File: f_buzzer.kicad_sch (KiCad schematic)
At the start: 11 parts, among them J1 Conn_01x03, U1 SN74123N

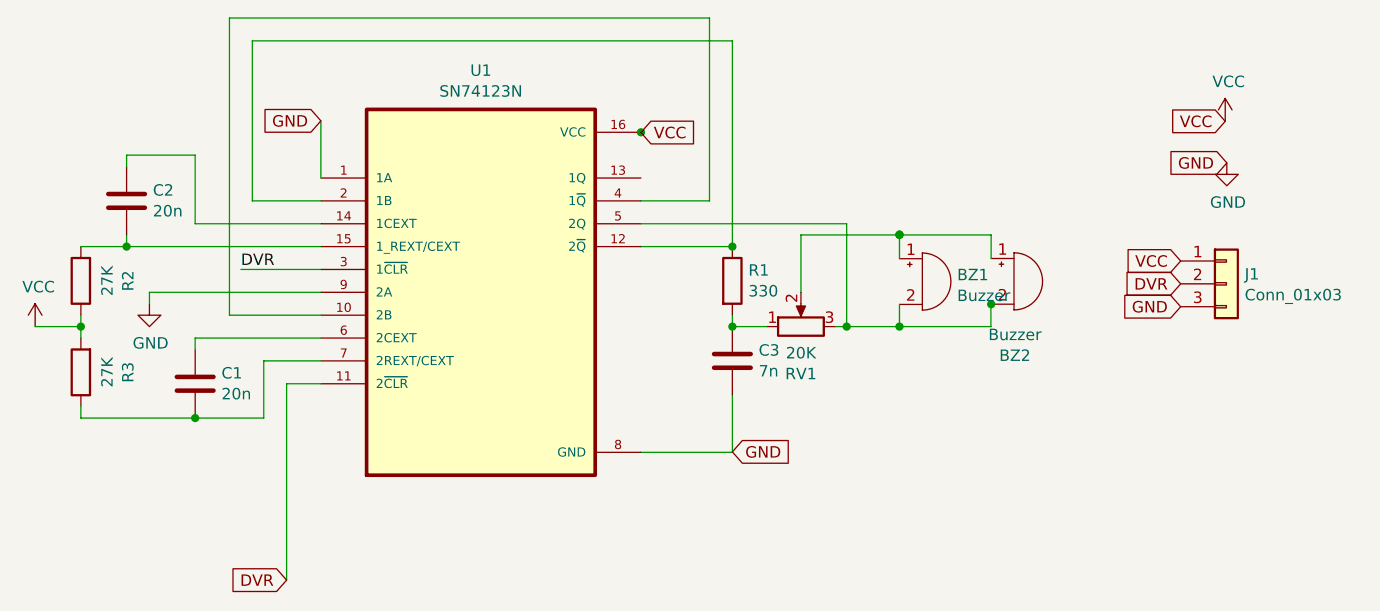
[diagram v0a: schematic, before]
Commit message: Rearranged the components
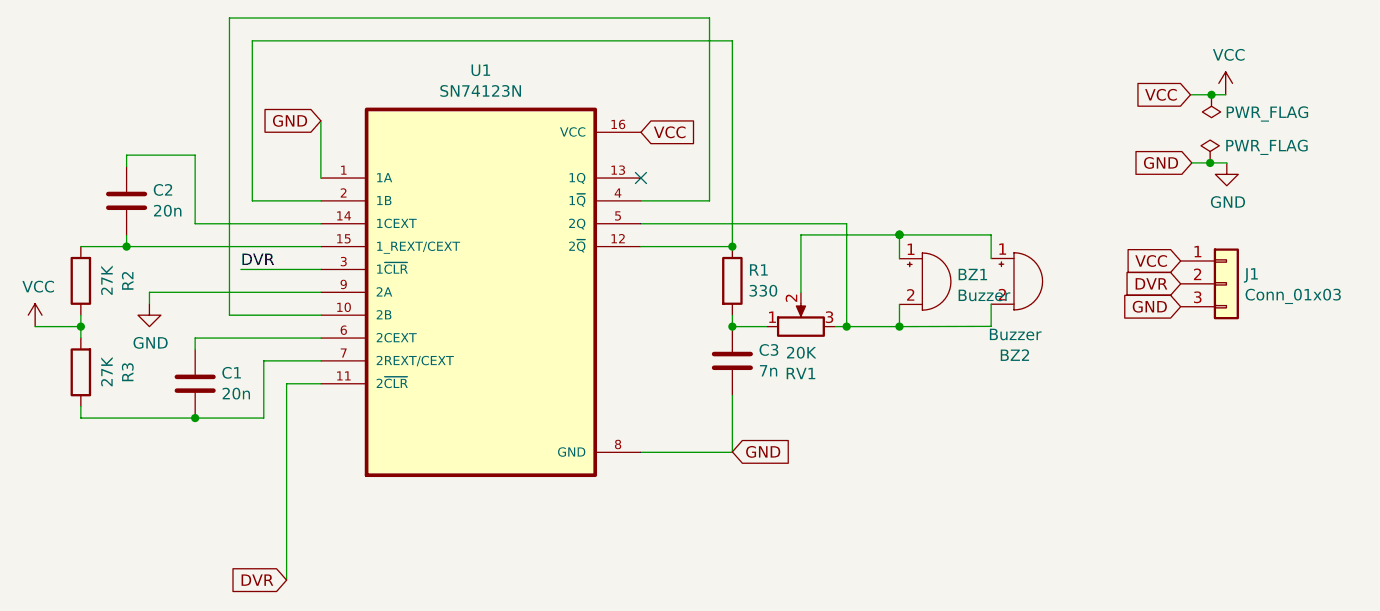
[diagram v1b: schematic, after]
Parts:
- RV1: symbol Device:R_POT -> Device:R_Potentiometer
- U1: footprint Package_DIP:DIP-16_W7.62mm -> Package_DIP:DIP-16_W7.62mm_Socket
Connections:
- net VCC: now also U1.16 (VCC)
- net at BZ2.2 (+): now also BZ1.2 (+), RV1.3, U1.5 (2Q)
- no-connect marks 0 -> 1
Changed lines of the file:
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@@
   (junction (at 114.3 116.84) (diameter 0) (color 0 0 0 0)
   )
+  (junction (at 227.2284 80.9244) (diameter 0) (color 0 0 0 0)
+  )
   (junction (at 173.99 106.68) (diameter 0) (color 0 0 0 0)
   )
-  (junction (at 163.83 85.09) (diameter 0) (color 0 0 0 0)
-  )
   (junction (at 192.5574 96.4946) (diameter 0) (color 0 0 0 0)
   )
@@
   (junction (at 192.5574 106.68) (diameter 0) (color 0 0 0 0)
   )
-  (junction (at 202.7428 104.1908) (diameter 0) (color 0 0 0 0)
+  (junction (at 227.076 88.4936) (diameter 0) (color 0 0 0 0)
   )
   (junction (at 101.6 106.68) (diameter 0) (color 0 0 0 0)
   )
+  (no_connect (at 163.83 90.17))
   (wire (pts (xy 128.27 113.03) (xy 124.46 113.03))
     (stroke (width 0) (type default) (color 0 0 0 0))
@@
     (stroke (width 0) (type default) (color 0 0 0 0))
   )
+  (wire (pts (xy 224.8916 80.9244) (xy 227.2284 80.9244))
+    (stroke (width 0) (type default) (color 0 0 0 0))
+  )
+  (wire (pts (xy 227.076 88.4936) (xy 228.9302 88.4936))
+    (stroke (width 0) (type default) (color 0 0 0 0))
+  )
   (wire (pts (xy 181.61 96.4946) (xy 181.61 102.87))
     (stroke (width 0) (type default) (color 0 0 0 0))
@@
     (stroke (width 0) (type default) (color 0 0 0 0))
   )
+  (wire (pts (xy 227.2284 80.9244) (xy 228.8032 80.9244))
+    (stroke (width 0) (type default) (color 0 0 0 0))
+  )
   (wire (pts (xy 124.46 113.03) (xy 124.46 134.8486))
     (stroke (width 0) (type default) (color 0 0 0 0))
@@
     (stroke (width 0) (type default) (color 0 0 0 0))
   )
-  (wire (pts (xy 202.7174 106.68) (xy 202.7174 104.2162))
+  (wire (pts (xy 202.7428 106.6546) (xy 202.7428 104.1908))
     (stroke (width 0) (type default) (color 0 0 0 0))
   )
@@
     (stroke (width 0) (type default) (color 0 0 0 0))
   )
-  (wire (pts (xy 192.5574 106.68) (xy 202.7174 106.68))
+  (wire (pts (xy 192.5574 106.68) (xy 202.7428 106.6546))
     (stroke (width 0) (type default) (color 0 0 0 0))
   )
@@
     (stroke (width 0) (type default) (color 0 0 0 0))
   )
-  (wire (pts (xy 163.7792 85.0646) (xy 163.7792 85.09))
-    (stroke (width 0) (type default) (color 0 0 0 0))
-  )
   (wire (pts (xy 163.83 95.25) (xy 186.69 95.25))
     (stroke (width 0) (type default) (color 0 0 0 0))
   )
-  (wire (pts (xy 163.7792 85.09) (xy 163.7284 85.09))
+  (wire (pts (xy 225.044 88.4936) (xy 227.076 88.4936))
     (stroke (width 0) (type default) (color 0 0 0 0))
   )
@@
     )
   )
-  (global_label "GND" (shape input) (at 228.9302 88.4936 180) (fields_autoplaced)
+  (global_label "GND" (shape input) (at 225.044 88.4936 180) (fields_autoplaced)
+    (effects (font (size 1.27 1.27)) (justify right))
+    (property "Intersheet References" "${INTERSHEET_REFS}" (id 0) (at -3.8862 0 0)
+      (effects (font (size 1.27 1.27)) hide)
+    )
+  )
+  (global_label "GND" (shape input) (at 223.7994 104.4702 180) (fields_autoplaced)
     (effects (font (size 1.27 1.27)) (justify right))
     (property "Intersheet References" "${INTERSHEET_REFS}" (id 0) (at 0 0 0)
@@
     )
   )
-  (global_label "GND" (shape input) (at 223.7994 104.4702 180) (fields_autoplaced)
+  (global_label "DVR" (shape input) (at 223.7994 101.9302 180) (fields_autoplaced)
     (effects (font (size 1.27 1.27)) (justify right))
     (property "Intersheet References" "${INTERSHEET_REFS}" (id 0) (at 0 0 0)
@@
     )
   )
-  (global_label "DVR" (shape input) (at 223.7994 101.9302 180) (fields_autoplaced)
+  (global_label "GND" (shape input) (at 128.27 83.82 180) (fields_autoplaced)
     (effects (font (size 1.27 1.27)) (justify right))
     (property "Intersheet References" "${INTERSHEET_REFS}" (id 0) (at 0 0 0)
@@
     )
   )
-  (global_label "GND" (shape input) (at 128.27 83.82 180) (fields_autoplaced)
-    (effects (font (size 1.27 1.27)) (justify right))
-    (property "Intersheet References" "${INTERSHEET_REFS}" (id 0) (at 0 0 0)
-      (effects (font (size 1.27 1.27)) hide)
-    )
-  )
-  (global_label "VCC" (shape input) (at 228.7524 83.8708 180) (fields_autoplaced)
-    (effects (font (size 1.27 1.27)) (justify right))
-    (property "Intersheet References" "${INTERSHEET_REFS}" (id 0) (at 0 0 0)
-      (effects (font (size 1.27 1.27)) hide)
-    )
-  )
-  (global_label "VCC" (shape input) (at 163.83 85.1154 0) (fields_autoplaced)
+  (global_label "VCC" (shape input) (at 224.8916 80.9244 180) (fields_autoplaced)
+    (effects (font (size 1.27 1.27)) (justify right))
+    (property "Intersheet References" "${INTERSHEET_REFS}" (id 0) (at -3.8608 -2.9464 0)
+      (effects (font (size 1.27 1.27)) hide)
+    )
+  )
+  (global_label "VCC" (shape input) (at 163.83 85.09 0) (fields_autoplaced)
     (effects (font (size 1.27 1.27)) (justify left))
-    (property "Intersheet References" "${INTERSHEET_REFS}" (id 0) (at 0 0 0)
+    (property "Intersheet References" "${INTERSHEET_REFS}" (id 0) (at 0 -0.0254 0)
       (effects (font (size 1.27 1.27)) hide)
     )
@@
     (pin "2")
   )
-  (symbol (lib_id "Device:R_POT") (at 181.61 106.68 90) (unit 1)
+  (symbol (lib_id "Device:R_Potentiometer") (at 181.61 106.68 90) (unit 1)
     (in_bom yes) (on_board yes)
     (property "Reference" "RV1" (id 0) (at 181.61 111.9378 90))
@@
     (property "Reference" "U1" (id 0) (at 146.05 78.232 0))
     (property "Value" "SN74123N" (id 1) (at 146.05 80.5434 0))
-    (property "Footprint" "Package_DIP:DIP-16_W7.62mm" (id 2) (at 146.05 102.87 0)
+    (property "Footprint" "Package_DIP:DIP-16_W7.62mm_Socket" (id 2) (at 146.05 102.87 0)
       (effects (font (size 1.27 1.27)) (justify left bottom) hide)
     )
@@
     (pin "3")
   )
-  (symbol (lib_id "power:VCC") (at 228.7524 83.8708 0) (unit 1)
-    (in_bom yes) (on_board yes)
-    (property "Reference" "#PWR?" (id 0) (at 228.7524 87.6808 0)
-      (effects (font (size 1.27 1.27)) hide)
-    )
-    (property "Value" "VCC" (id 1) (at 229.1334 79.4766 0))
-    (property "Footprint" "" (id 2) (at 228.7524 83.8708 0)
-      (effects (font (size 1.27 1.27)) hide)
-    )
-    (property "Datasheet" "" (id 3) (at 228.7524 83.8708 0)
+  (symbol (lib_id "power:VCC") (at 228.8032 80.9244 0) (unit 1)
+    (in_bom yes) (on_board yes)
+    (property "Reference" "#PWR0101" (id 0) (at 228.8032 84.7344 0)
+      (effects (font (size 1.27 1.27)) hide)
+    )
+    (property "Value" "VCC" (id 1) (at 229.1842 76.5302 0))
+    (property "Footprint" "" (id 2) (at 228.8032 80.9244 0)
+      (effects (font (size 1.27 1.27)) hide)
+    )
+    (property "Datasheet" "" (id 3) (at 228.8032 80.9244 0)
       (effects (font (size 1.27 1.27)) hide)
     )
@@
   (symbol (lib_id "power:GND") (at 228.9302 88.4936 0) (unit 1)
     (in_bom yes) (on_board yes)
-    (property "Reference" "#PWR?" (id 0) (at 228.9302 94.8436 0)
+    (property "Reference" "#PWR0102" (id 0) (at 228.9302 94.8436 0)
       (effects (font (size 1.27 1.27)) hide)
     )
@@
     (pin "1")
   )
+  (symbol (lib_id "power:PWR_FLAG") (at 227.076 88.4936 0) (unit 1)
+    (in_bom yes) (on_board yes)
+    (property "Reference" "#FLG0101" (id 0) (at 227.076 86.5886 0)
+      (effects (font (size 1.27 1.27)) hide)
+    )
+    (property "Value" "PWR_FLAG" (id 1) (at 233.3752 86.614 0))
+    (property "Footprint" "" (id 2) (at 227.076 88.4936 0)
+      (effects (font (size 1.27 1.27)) hide)
+    )
+    (property "Datasheet" "~" (id 3) (at 227.076 88.4936 0)
+      (effects (font (size 1.27 1.27)) hide)
+    )
+    (pin "1")
+  )
+  (symbol (lib_id "power:PWR_FLAG") (at 227.2284 80.9244 180) (unit 1)
+    (in_bom yes) (on_board yes)
+    (property "Reference" "#FLG0102" (id 0) (at 227.2284 82.8294 0)
+      (effects (font (size 1.27 1.27)) hide)
+    )
+    (property "Value" "PWR_FLAG" (id 1) (at 233.426 82.9056 0))
+    (property "Footprint" "" (id 2) (at 227.2284 80.9244 0)
+      (effects (font (size 1.27 1.27)) hide)
+    )
+    (property "Datasheet" "~" (id 3) (at 227.2284 80.9244 0)
+      (effects (font (size 1.27 1.27)) hide)
+    )
+    (pin "1")
+  )
   (sheet_instances
     (path "/" (page "1"))
   )
   (symbol_instances
+    (path "/7bf3ae51-501e-48a7-a2bf-a4a318e05ebf"
+      (reference "#FLG0101") (unit 1) (value "PWR_FLAG") (footprint "")
+    )
+    (path "/8416c9e8-3c1c-41a1-b9f1-9967a7a1981f"
+      (reference "#FLG0102") (unit 1) (value "PWR_FLAG") (footprint "")
+    )
+    (path "/00000000-0000-0000-0000-000060439457"
+      (reference "#PWR0101") (unit 1) (value "VCC") (footprint "")
+    )
+    (path "/00000000-0000-0000-0000-000060439cfe"
+      (reference "#PWR0102") (unit 1) (value "GND") (footprint "")
+    )
     (path "/00000000-0000-0000-0000-000060206601"
       (reference "#PWR0103") (unit 1) (value "GND") (footprint "")
@@
       (reference "#PWR0104") (unit 1) (value "VCC") (footprint "")
     )
-    (path "/00000000-0000-0000-0000-000060439457"
-      (reference "#PWR?") (unit 1) (value "VCC") (footprint "")
-    )
-    (path "/00000000-0000-0000-0000-000060439cfe"
-      (reference "#PWR?") (unit 1) (value "GND") (footprint "")
-    )
     (path "/00000000-0000-0000-0000-0000602085cd"
       (reference "BZ1") (unit 1) (value "Buzzer") (footprint "f_buzzer:buzzer_bottom")
@@
     )
     (path "/00000000-0000-0000-0000-0000601f7510"
-      (reference "U1") (unit 1) (value "SN74123N") (footprint "Package_DIP:DIP-16_W7.62mm")
-    )
-  )
+      (reference "U1") (unit 1) (value "SN74123N") (footprint "Package_DIP:DIP-16_W7.62mm_Socket")
+    )
+  )
